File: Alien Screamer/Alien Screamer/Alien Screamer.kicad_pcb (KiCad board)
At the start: 4 copper layers, 108 x 79 mm, 62 parts, among them J1 AudioJack2, Q1 2N3904, Q2 2N3904, Q3 NJFET, SW1 PWR, SW2 LFO_Shaping, SW3 LFO_Shaping, SW4 SYNC, U1 LM324, U2 LM386

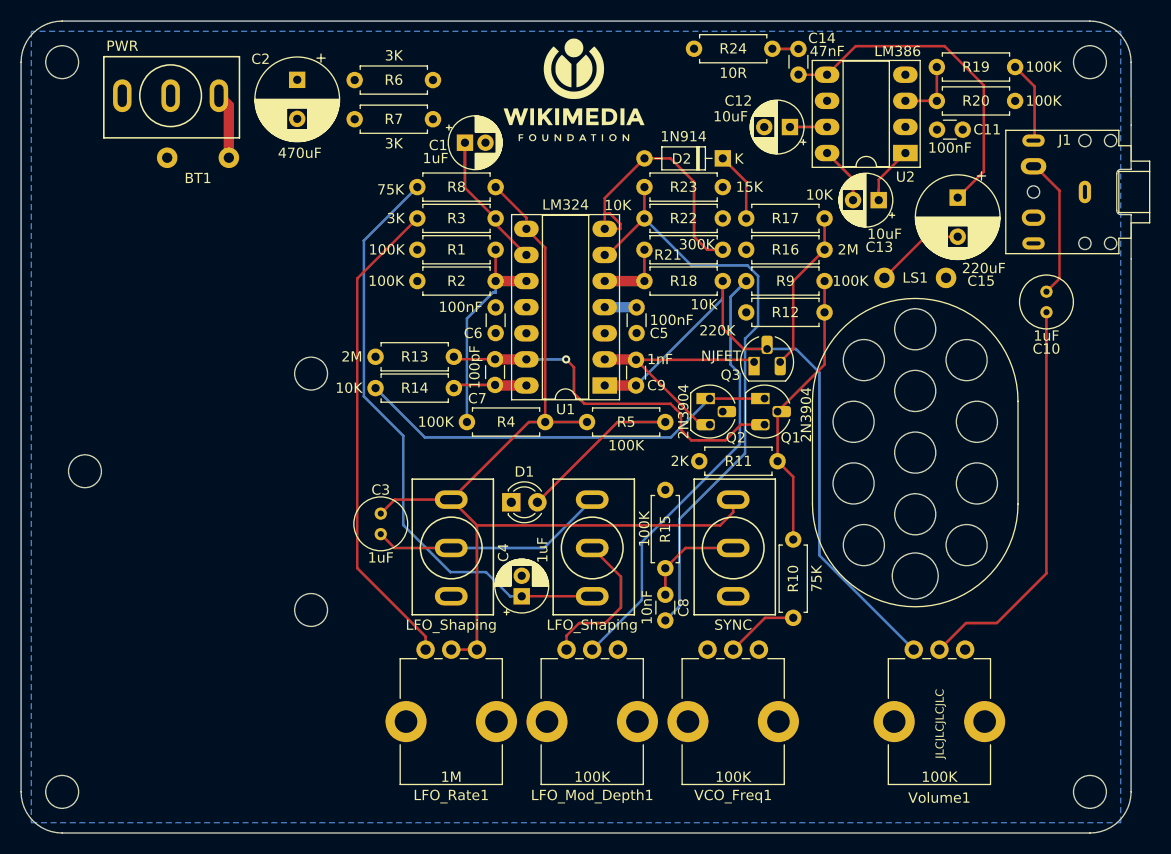
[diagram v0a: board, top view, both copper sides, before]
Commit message: Alien Screamer - changed resistors sizes
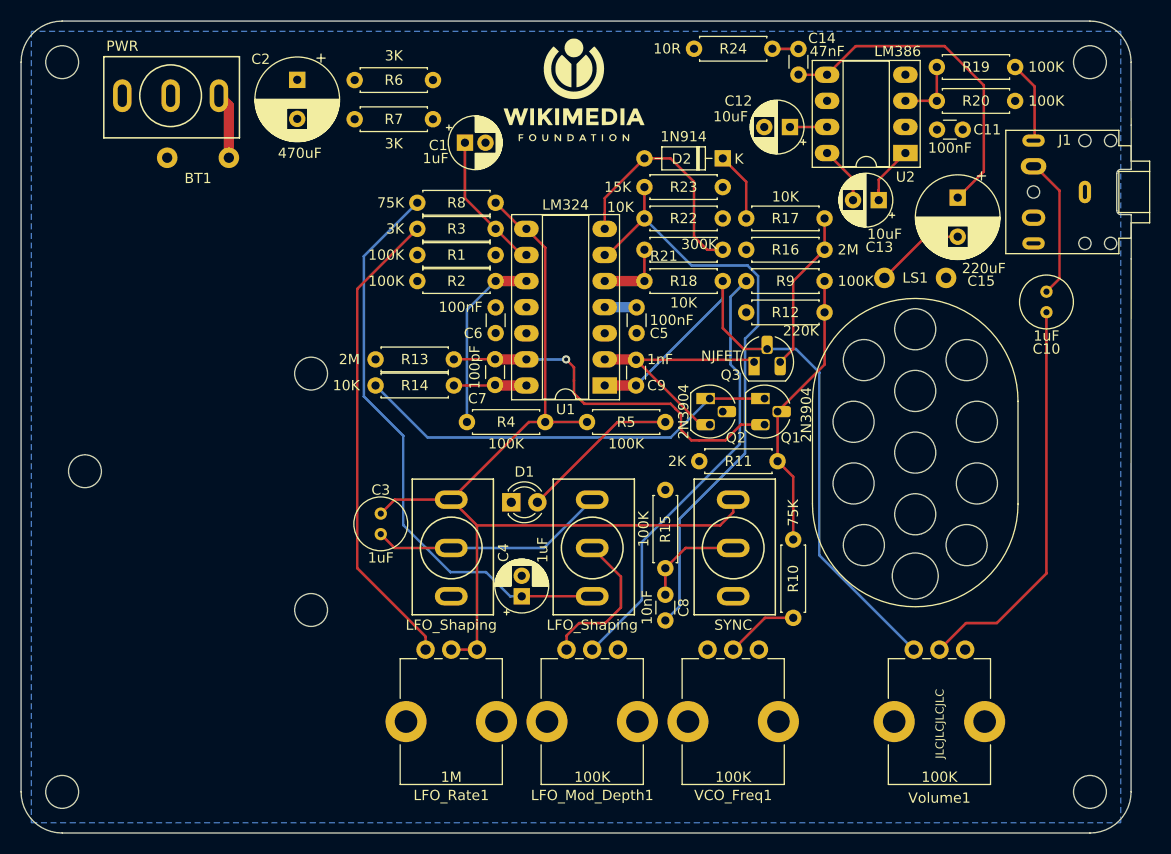
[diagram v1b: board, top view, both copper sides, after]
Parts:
- R1, R10, R11, R12, R13, R14, R15, R16, R17, R18, R19, R2, R20, R21, R22, R23, R24, R3, R4, R5, R6, R7, R8, R9: footprint Resistor_THT:R_Axial_DIN0207_L6.3mm_D2.5mm_P7.62mm_Horizontal -> Library:R_Axial_DIN0207_L6.3mm_D2.5mm_P7.62mm_Horizontal
- moved R8 1.52 mm to (114.6, 90.7)
- moved R3 1.02 mm to (122.2, 93.2)
- moved R1 0.51 mm to (122.2, 95.8)
- moved R13 0.25 mm to (118.1, 105.9)
- moved R14 0.25 mm to (110.5, 108.5)
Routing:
- net Net-(D2-A): track 26.8 -> 22.9 mm
- net Net-(U1C-+): track 21.1 -> 17.9 mm
- net Net-(U1C--): track 15.6 -> 13.7 mm
- net X5: track 57.9 -> 56.4 mm
- net X1: track 47.1 -> 46.1 mm
- net X3: track 94.0 -> 93.2 mm

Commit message: AlienScream - fixed a few values
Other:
- board text added: "+"
- board text added: "-"
- board text added: "C13 Optional"
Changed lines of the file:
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@@
     (effects (font (size 1.5 1.5) (thickness 0.3) bold) (justify mirror))
+  )
+  (gr_text "C13 Optional" (at 146 89) (layer "F.SilkS")
+    (effects (font (size 1 1) (thickness 0.15)) (justify left bottom))
+  )
+  (gr_text "-" (at 88 86.5) (layer "F.SilkS")
+    (effects (font (size 1 1) (thickness 0.15)))
   )
   (gr_text "JLCJLCJLCJLC" (at 165.862 144.78 90) (layer "F.SilkS")
     (effects (font (size 0.8 0.8) (thickness 0.15)) (justify left bottom))
+  )
+  (gr_text "+" (at 98.5 86.5) (layer "F.SilkS")
+    (effects (font (size 1 1) (thickness 0.15)))
   )
   (gr_text_box "Data Platform Engineering\nOffsite - 2024\nWMF"
@@
       (effects (font (size 1.5 1.5) (thickness 0.3) bold) (justify top))
   )
-  (gr_text_box "Alien Screamer\n\nMusic From Outer Space\nhttps://musicfromouterspace.com/"
+  (gr_text_box "Alien Screamer - V2\n\nMusic From Outer Space\nhttps://musicfromouterspace.com/"
     (start 85.852 126.365) (end 94.234 106.299) (angle 90) (layer "F.SilkS")
       (effects (font (size 1.5 1.5) (thickness 0.3) bold) (justify top))

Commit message: Alien Screamer - misc fixes
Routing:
- net Net-(U1C-+): track 17.9 -> 20.4 mm
- net X3: track 93.2 -> 91.7 mm
- net Net-(Q2-C): track 24.4 -> 23.2 mm
- net X5: track 56.4 -> 57.5 mm
- net Net-(Q1-C): track 36.9 -> 36.2 mm
- added copper zone on F.Cu, net BN
- added copper zone on In2.Cu, net GND
- removed copper zone on In2.Cu, net BN
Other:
- board text added: "OFF"
- board text added: "ON"

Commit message: minor fixes and cleanups
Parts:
- added J2: Conn_01x03, Connector_PinHeader_2.54mm:PinHeader_1x03_P2.54mm_Vertical, F.Cu at (119.4, 75.9)
- LFO_SHAPING1: renamed from SW2; value LFO_Shaping -> SW_SPDT
- LFO_SHAPING2: renamed from SW3; value LFO_Shaping -> SW_SPDT
- PWR1: renamed from SW1; value PWR -> SW_SPDT
- Q3: value NJFET -> 2N5457
- R20, R5: value 100K -> 4.7K
- R6, R7: value 3K -> 4.7K
- SYNC1: renamed from SW4; value SYNC -> SW_SPDT
- moved C4 17.3 mm to (111.3, 118.1)
- moved LFO_SHAPING2 16.8 mm to (114.9, 126.5), turned to -90 degrees
- moved LFO_SHAPING1 13.7 mm to (131.6, 124.3)
- moved C3 6.37 mm to (116.1, 117.1), turned to 0 degrees
- moved D1 2.73 mm to (123.7, 117.1)
- moved G*** 1.27 mm to (131.1, 79.8)
- turned SYNC1 to 180 degrees
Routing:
- net X3: track 91.7 -> 112.0 mm
- net X5: track 57.5 -> 41.4 mm
- net Net-(LFO_SHAPING2-B): track 14.7 -> 17.3 mm
- net B+: track 6.44 -> 8.12 mm
- net X1: track 46.1 -> 47.3 mm
- net X7: track 15.7 -> 14.6 mm
- net Net-(LFO_SHAPING1-B): track 23.1 -> 22.0 mm
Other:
- board text added: "BN"
- board text added: "BP"
- board text added: "GND"
- board text removed: "+"
- board text removed: "-"

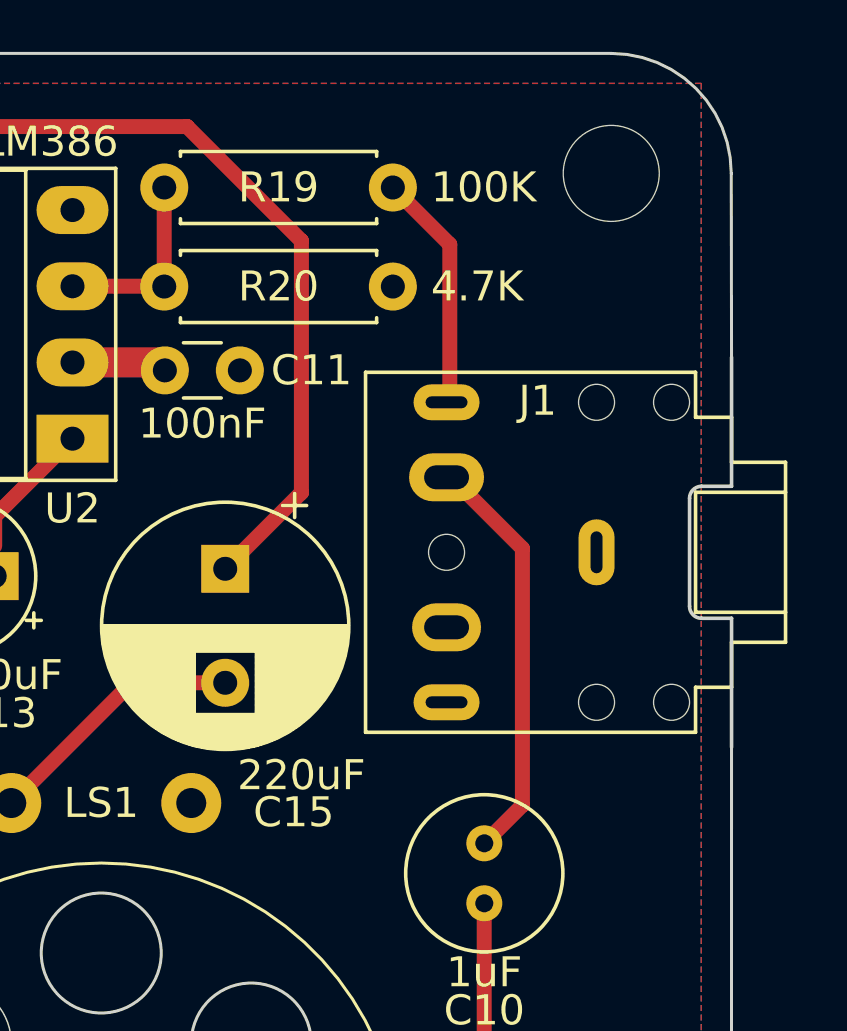
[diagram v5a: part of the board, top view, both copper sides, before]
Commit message: Alien Screamer - fix audio jack
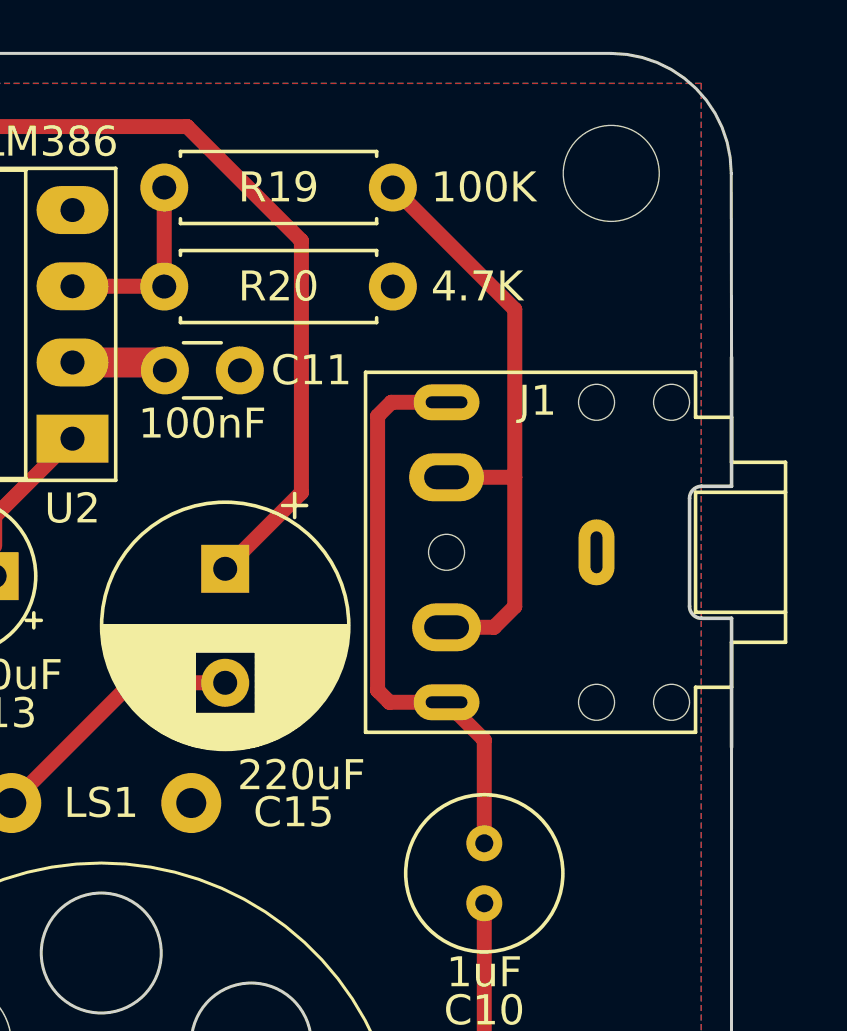
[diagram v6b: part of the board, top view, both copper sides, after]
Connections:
- J1 pad R: (no net) -> Net-(C10-Pad2)
- J1 pad RN: (no net) -> Net-(J1-PadRN)
- J1 pad T: Net-(J1-PadT) -> Net-(C10-Pad2)
- J1 pad TN: Net-(C10-Pad2) -> Net-(J1-PadRN)
- R19 pad 2: Net-(J1-PadT) -> Net-(J1-PadRN)
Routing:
- net Net-(J1-PadRN): track 0.00 -> 20.5 mm
- net Net-(J1-PadT): track 7.90 -> 0.00 mm
- net Net-(C10-Pad2): track 13.8 -> 19.3 mm

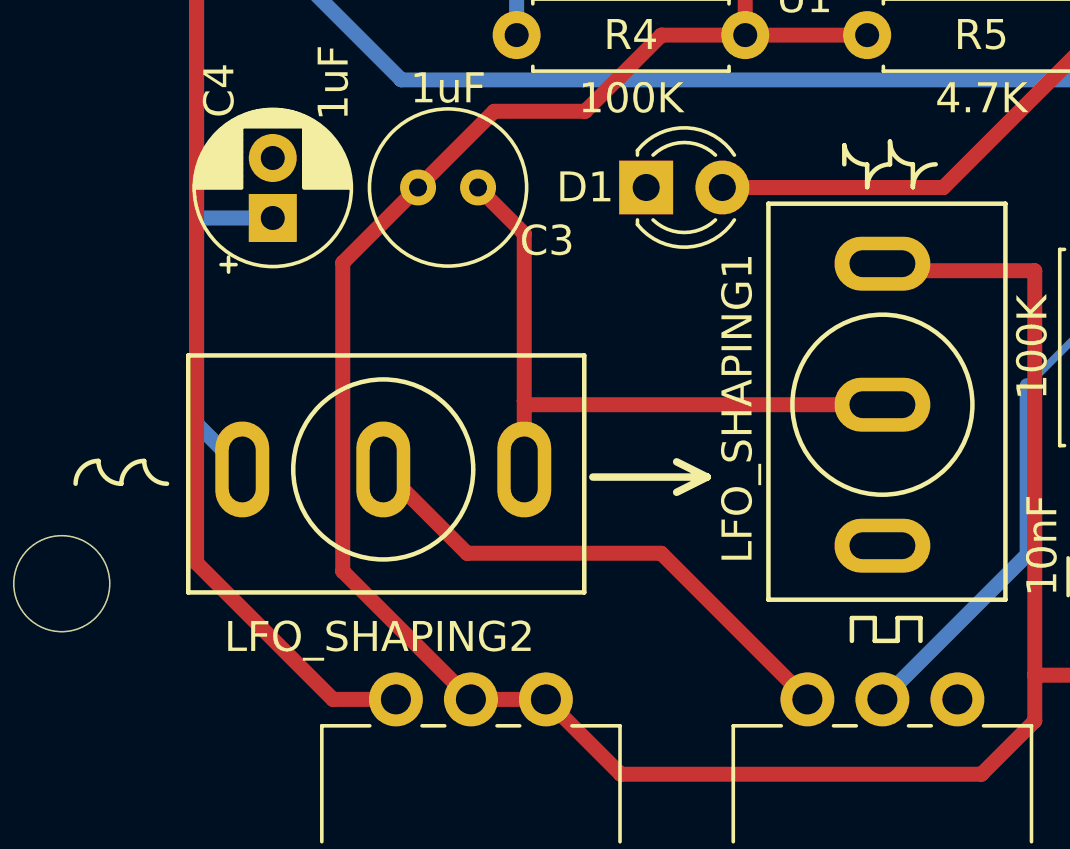
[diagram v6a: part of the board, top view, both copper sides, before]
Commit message: Alien Screamer - fix switch orientation and remove optional components
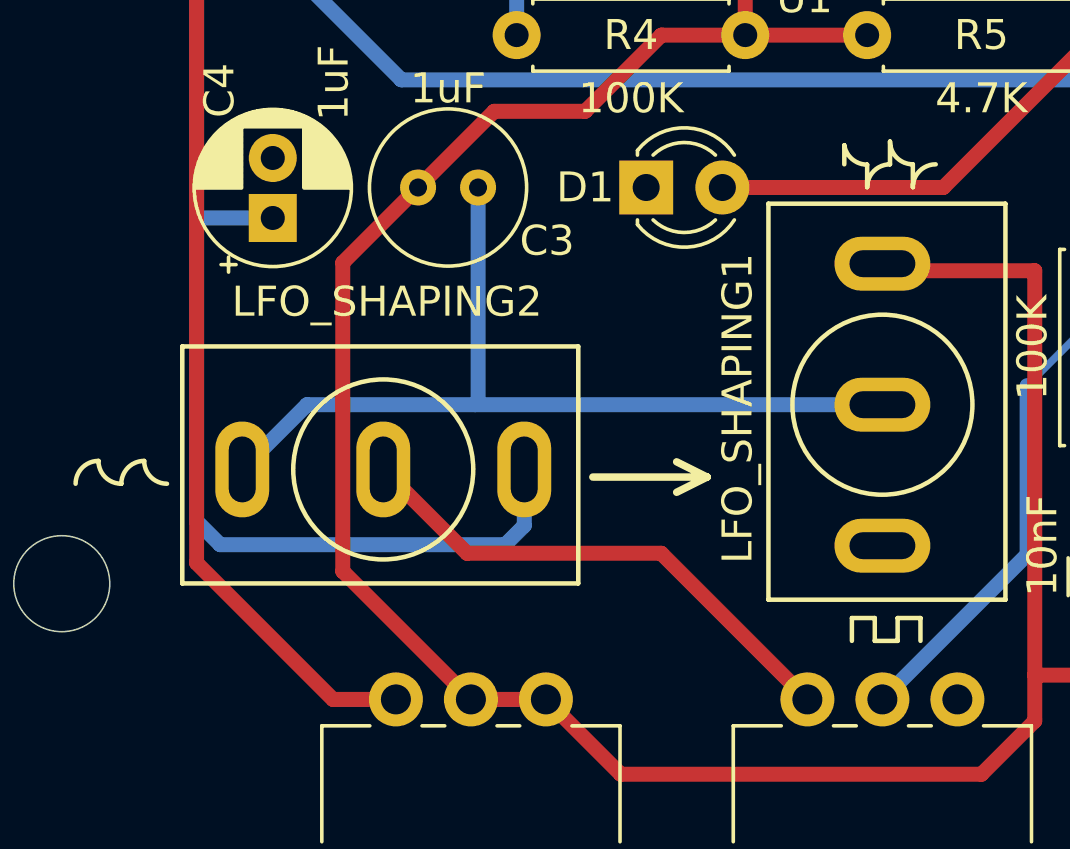
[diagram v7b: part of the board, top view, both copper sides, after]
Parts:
- turned LFO_SHAPING2 to 90 degrees
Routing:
- net X5: track 41.4 -> 55.9 mm
- net Net-(LFO_SHAPING1-B): track 22.0 -> 29.4 mm
